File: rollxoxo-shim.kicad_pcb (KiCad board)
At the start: 4 copper layers, 29 x 42 mm, 68 parts, among them J1 USB_C_Receptacle_USB2.0_14P, J2 Conn_01x02, J3 Conn_01x10, J4 Conn_01x01, J5 Conn_01x10, J6 Conn_01x03, J7 Conn_01x01, SW1 SW_Push, SW2 SW_Push, U1 SN74LV1T125DBV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

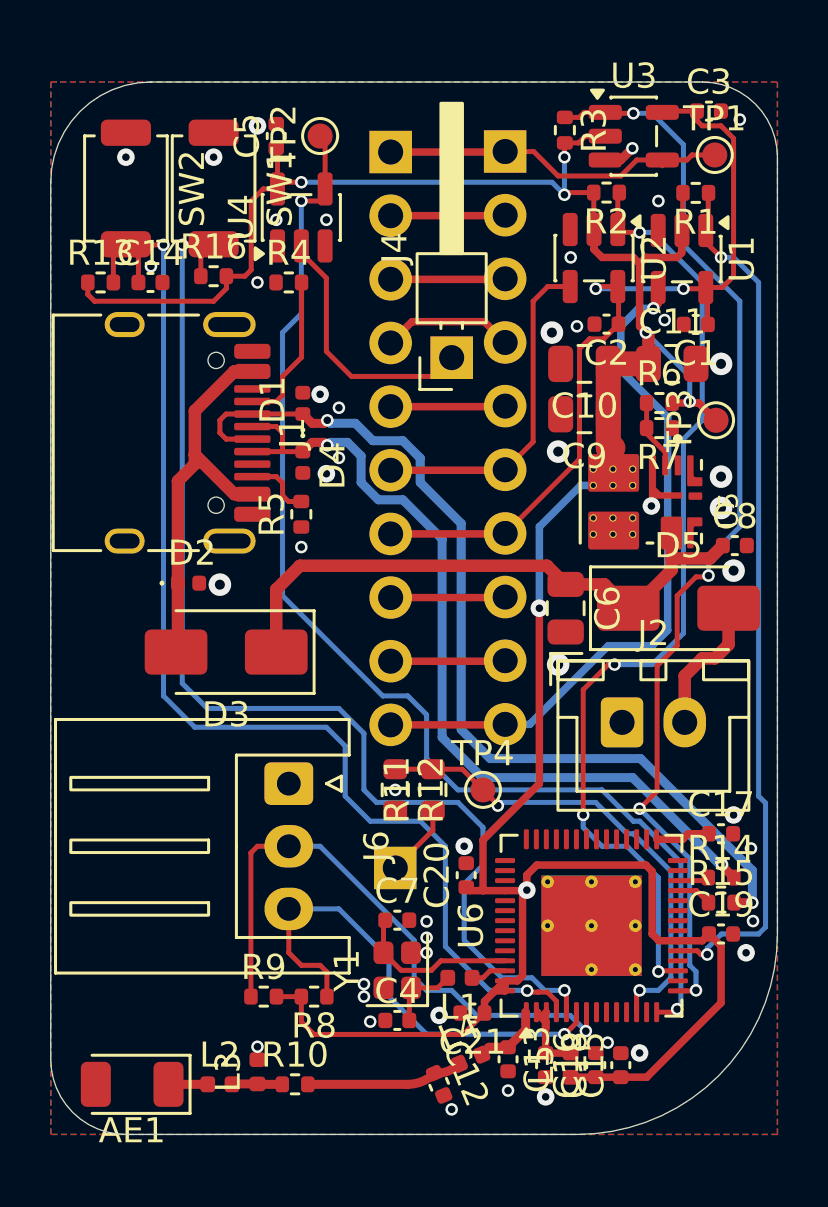
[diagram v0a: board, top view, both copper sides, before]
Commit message: pcb: add stiching vias
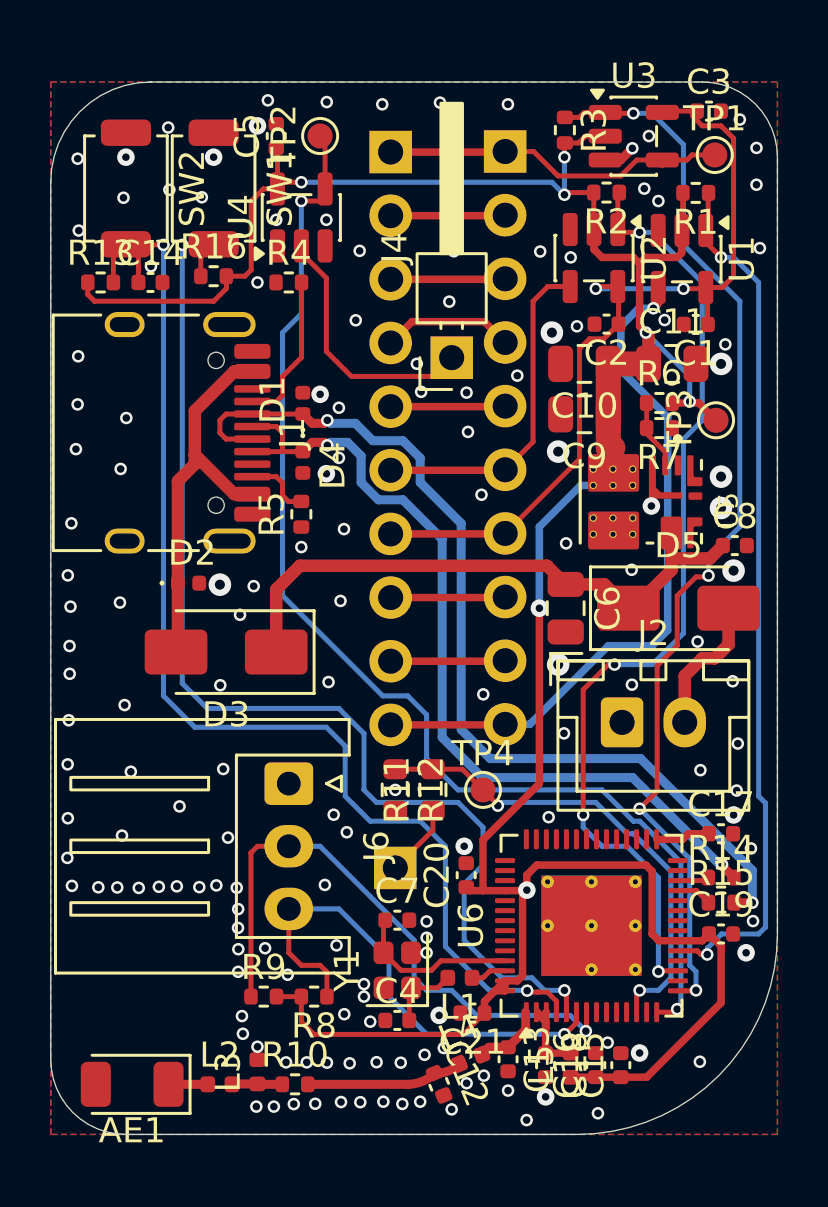
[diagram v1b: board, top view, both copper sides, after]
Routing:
- net GND: vias 46 -> 158

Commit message: pcb: run and fix DRC
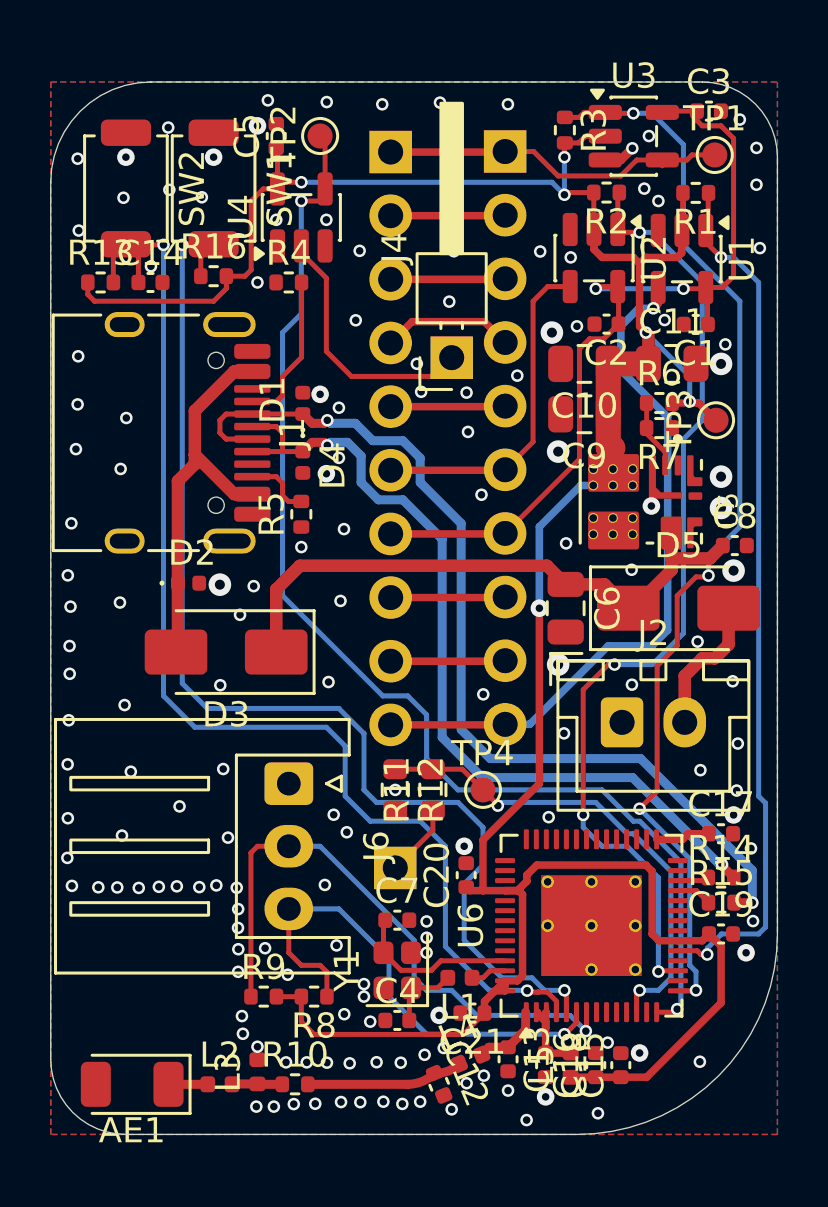
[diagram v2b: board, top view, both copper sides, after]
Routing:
- net +3V3: track 112.0 -> 112.3 mm, vias 7 -> 6
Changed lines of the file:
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@@
 			(at -1.75 0 90)
 			(size 0.5 0.5)
-			(drill 0.2)
+			(drill 0.3)
 			(property pad_prop_heatsink)
 			(layers "*.Cu")
@@
 			(at -1.75 1.75 90)
 			(size 0.5 0.5)
-			(drill 0.2)
+			(drill 0.3)
 			(property pad_prop_heatsink)
 			(layers "*.Cu")
@@
 			(at 0 -1.75 90)
 			(size 0.5 0.5)
-			(drill 0.2)
+			(drill 0.3)
 			(property pad_prop_heatsink)
 			(layers "*.Cu")
@@
 			(at 0 0 90)
 			(size 0.5 0.5)
-			(drill 0.2)
+			(drill 0.3)
 			(property pad_prop_heatsink)
 			(layers "*.Cu")
@@
 			(at 0 1.75 90)
 			(size 0.5 0.5)
-			(drill 0.2)
+			(drill 0.3)
 			(property pad_prop_heatsink)
 			(layers "*.Cu")
@@
 			(at 1.75 -1.75 90)
 			(size 0.5 0.5)
-			(drill 0.2)
+			(drill 0.3)
 			(property pad_prop_heatsink)
 			(layers "*.Cu")
@@
 			(at 1.75 0 90)
 			(size 0.5 0.5)
-			(drill 0.2)
+			(drill 0.3)
 			(property pad_prop_heatsink)
 			(layers "*.Cu")
@@
 			(at 1.75 1.75 90)
 			(size 0.5 0.5)
-			(drill 0.2)
+			(drill 0.3)
 			(property pad_prop_heatsink)
 			(layers "*.Cu")
@@
 		(pad "4" thru_hole circle
 			(at -1.3 0.325 270)
-			(size 0.3 0.3)
-			(drill 0.2)
+			(size 0.4 0.4)
+			(drill 0.3)
 			(layers "*.Cu")
 			(remove_unused_layers no)
@@
 		(pad "4" thru_hole circle
 			(at -1.3 1.113 270)
-			(size 0.3 0.3)
-			(drill 0.2)
+			(size 0.4 0.4)
+			(drill 0.3)
 			(layers "*.Cu")
 			(remove_unused_layers no)
@@
 		(pad "4" thru_hole circle
 			(at -1.3 1.9 270)
-			(size 0.3 0.3)
-			(drill 0.2)
+			(size 0.4 0.4)
+			(drill 0.3)
 			(layers "*.Cu")
 			(remove_unused_layers no)
@@
 		(pad "4" thru_hole circle
 			(at -0.65 0.325 270)
-			(size 0.3 0.3)
-			(drill 0.2)
+			(size 0.4 0.4)
+			(drill 0.3)
 			(layers "*.Cu")
 			(remove_unused_layers no)
@@
 		(pad "4" thru_hole circle
 			(at -0.65 1.113 270)
-			(size 0.3 0.3)
-			(drill 0.2)
+			(size 0.4 0.4)
+			(drill 0.3)
 			(layers "*.Cu")
 			(remove_unused_layers no)
@@
 		(pad "4" thru_hole circle
 			(at -0.65 1.9 270)
-			(size 0.3 0.3)
-			(drill 0.2)
+			(size 0.4 0.4)
+			(drill 0.3)
 			(layers "*.Cu")
 			(remove_unused_layers no)
@@
 		(pad "5" thru_hole circle
 			(at 0.65 0.325 270)
-			(size 0.3 0.3)
-			(drill 0.2)
+			(size 0.4 0.4)
+			(drill 0.3)
 			(layers "*.Cu")
 			(remove_unused_layers no)
@@
 		(pad "5" thru_hole circle
 			(at 0.65 1.113 270)
-			(size 0.3 0.3)
-			(drill 0.2)
+			(size 0.4 0.4)
+			(drill 0.3)
 			(layers "*.Cu")
 			(remove_unused_layers no)
@@
 		(pad "5" thru_hole circle
 			(at 0.65 1.9 270)
-			(size 0.3 0.3)
-			(drill 0.2)
+			(size 0.4 0.4)
+			(drill 0.3)
 			(layers "*.Cu")
 			(remove_unused_layers no)
@@
 		(pad "5" thru_hole circle
 			(at 1.3 0.325 270)
-			(size 0.3 0.3)
-			(drill 0.2)
+			(size 0.4 0.4)
+			(drill 0.3)
 			(layers "*.Cu")
 			(remove_unused_layers no)
@@
 		(pad "5" thru_hole circle
 			(at 1.3 1.113 270)
-			(size 0.3 0.3)
-			(drill 0.2)
+			(size 0.4 0.4)
+			(drill 0.3)
 			(layers "*.Cu")
 			(remove_unused_layers no)
@@
 		(pad "5" thru_hole circle
 			(at 1.3 1.9 270)
-			(size 0.3 0.3)
-			(drill 0.2)
+			(size 0.4 0.4)
+			(drill 0.3)
 			(layers "*.Cu")
 			(remove_unused_layers no)
@@
 	)
 	(segment
-		(start 73 150.25)
-		(end 73 149.65)
-		(width 0.3)
-		(layer "F.Cu")
-		(net "+3V3")
-	)
-	(segment
 		(start 62 125.5)
 		(end 61.75 125.75)
@@
 	)
 	(segment
+		(start 73 149.89636)
+		(end 73 149.65)
+		(width 0.3)
+		(layer "F.Cu")
+		(net "+3V3")
+	)
+	(segment
 		(start 77.75 128)
 		(end 77.5 127.75)
@@
 	)
 	(segment
-		(start 72.98 150.27)
-		(end 73 150.25)
-		(width 0.3)
-		(layer "F.Cu")
-		(net "+3V3")
-	)
-	(segment
 		(start 77.85 128.1)
 		(end 77.75 128)
@@
 	)
 	(segment
+		(start 72.62636 150.27)
+		(end 73 149.89636)
+		(width 0.3)
+		(layer "F.Cu")
+		(net "+3V3")
+	)
+	(segment
 		(start 61.75 125.75)
 		(end 61.01 125.75)
@@
 	)
 	(segment
+		(start 72.13 150.27)
+		(end 72.68 150.27)
+		(width 0.3)
+		(layer "F.Cu")
+		(net "+3V3")
+	)
+	(segment
 		(start 75.0675 120.4325)
 		(end 75.3375 120.1625)
@@
 	)
 	(segment
-		(start 72.83 150.42)
-		(end 73 150.25)
-		(width 0.3)
-		(layer "F.Cu")
-		(net "+3V3")
-	)
-	(segment
 		(start 72.13 153.87)
 		(end 72.62636 153.87)
@@
 	)
 	(segment
+		(start 72.68 150.27)
+		(end 72.83 150.42)
+		(width 0.3)
+		(layer "F.Cu")
+		(net "+3V3")
+	)
+	(segment
 		(start 78 152)
 		(end 78.27 152.27)
@@
 	)
 	(segment
-		(start 72.13 150.27)
-		(end 72.98 150.27)
-		(width 0.3)
-		(layer "F.Cu")
-		(net "+3V3")
-	)
-	(segment
 		(start 71.31 154.69)
 		(end 71.31 155.155)
@@
 	)
 	(segment
+		(start 72.13 150.27)
+		(end 72.62636 150.27)
+		(width 0.3)
+		(layer "F.Cu")
+		(net "+3V3")
+	)
+	(segment
 		(start 70.715 150.27)
 		(end 70.58 150.135)
@@
 		(size 0.7)
 		(drill 0.3)
-		(layers "F.Cu" "B.Cu")
-		(net "+3V3")
-	)
-	(via
-		(at 73 150.25)
-		(size 0.7)
-		(drill 0.3)
